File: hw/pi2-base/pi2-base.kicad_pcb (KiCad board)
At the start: 2 copper layers, 100 x 125 mm, 81 parts, among them J1 WAGO 2081-1122, J10 BUS Pull-down, J11 JUMPER3, J12 JUMPER3, J13 Power LEDs, J14 JUMPER3, J15 JUMPER3, J16 JUMPER3, J17 JUMPER3, J2 WAGO 243 orange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

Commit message: pi2-base revision 1 (prototypes ordered)
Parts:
- L1: value 220uH -> 100uH
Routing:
- net GND: track 0.00 -> 26.4 mm, vias 0 -> 9
- net (no net): track 5.74 -> 0.00 mm, vias 8 -> 0
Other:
- net class Power: via_dia 1 -> 1.2

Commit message: Changed resistor values from 56k/100k to 10k/18k of voltage divider of TXD and CTS
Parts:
- R10, R9: value 100k -> 18k
- R6, R7: value 56k -> 10k
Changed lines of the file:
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@@
-(kicad_pcb (version 20160815) (host pcbnew no-vcs-found)
+(kicad_pcb (version 20170123) (host pcbnew no-vcs-found-7600~57~ubuntu14.04.1)
   (general
     (links 173)
     (no_connects 0)
-    (area 73.305715 20.28 207.305716 164.789908)
+    (area 95.944999 32.404999 196.095001 157.555001)
     (thickness 1.6)
     (drawings 59)
@@
     (uvia_dia 0.3)
     (uvia_drill 0.1)
-    (diff_pair_gap 0.25)
-    (diff_pair_width 0.2)
     (add_net "/2 Relays/LEDVCC")
     (add_net "/2 Relays/REL1")
@@
     (uvia_dia 0.3)
     (uvia_drill 0.1)
-    (diff_pair_gap 0.25)
-    (diff_pair_width 0.2)
     (add_net /REL1_COM)
     (add_net /REL1_NC)
@@
     (uvia_dia 0.3)
     (uvia_drill 0.1)
-    (diff_pair_gap 0.25)
-    (diff_pair_width 0.2)
     (add_net +24V)
     (add_net +3.3V)
@@
       (effects (font (size 0.8 0.8) (thickness 0.15)) (justify mirror))
     )
-    (fp_text value 56k (at 0.127 -1.524 270) (layer B.Fab)
+    (fp_text value 10k (at 0.127 -1.524 270) (layer B.Fab)
       (effects (font (size 0.8 0.8) (thickness 0.15)) (justify mirror))
     )
@@
       (effects (font (size 0.8 0.8) (thickness 0.15)) (justify mirror))
     )
-    (fp_text value 56k (at 0.127 -1.524 270) (layer B.Fab)
+    (fp_text value 10k (at 0.127 -1.524 270) (layer B.Fab)
       (effects (font (size 0.8 0.8) (thickness 0.15)) (justify mirror))
     )
@@
       (effects (font (size 0.8 0.8) (thickness 0.15)) (justify mirror))
     )
-    (fp_text value 100k (at 0.127 -1.524 270) (layer B.Fab)
+    (fp_text value 18k (at 0.127 -1.524 270) (layer B.Fab)
       (effects (font (size 0.8 0.8) (thickness 0.15)) (justify mirror))
     )
@@
       (effects (font (size 0.8 0.8) (thickness 0.15)) (justify mirror))
     )
-    (fp_text value 100k (at 0.127 -1.524 270) (layer B.Fab)
-      (effects (font (size 0.8 0.8) (thickness 0.15)) (justify mirror))
-    )
+    (fp_text value 18k (at 0.127 -1.524 270) (layer B.Fab)
+      (effects (font (size 0.8 0.8) (thickness 0.15)) (justify mirror))
+    )

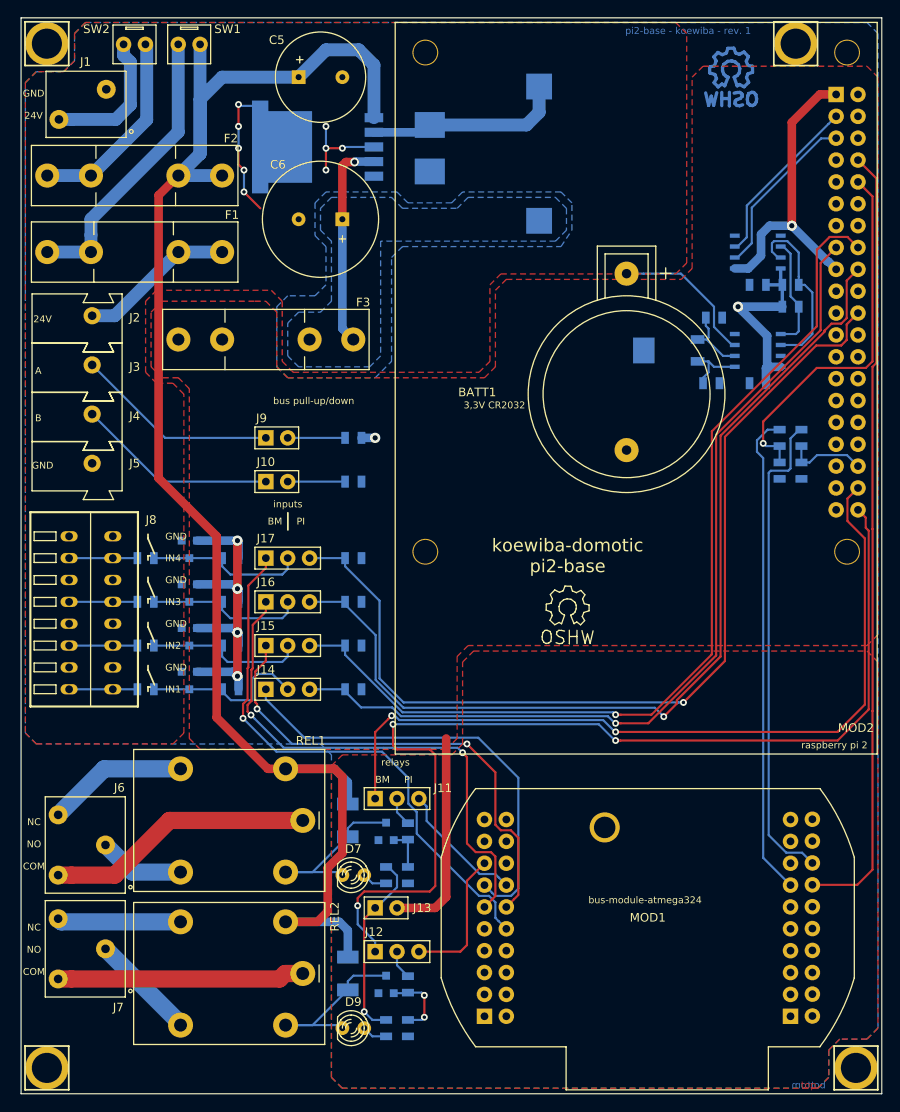
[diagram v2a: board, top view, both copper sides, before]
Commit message: Fix: Silkscreen jumper description Fix: Relay pinout
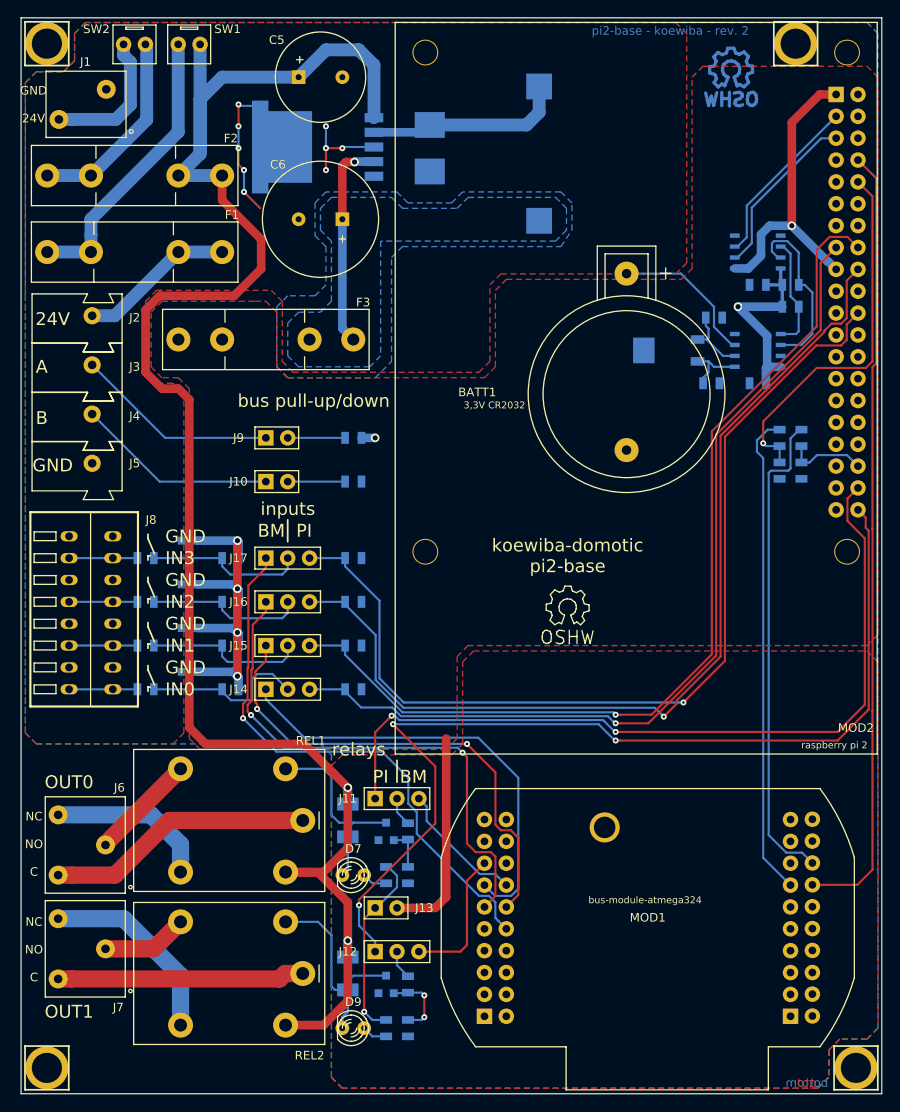
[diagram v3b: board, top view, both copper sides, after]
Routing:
- net +24V: track 183.9 -> 206.1 mm, vias 0 -> 2
- net /REL2_NC: track 14.4 -> 22.9 mm
- net /PI_REL2: track 121.0 -> 114.2 mm
- net Net-(D8-Pad1): track 21.4 -> 24.9 mm
- net Net-(D6-Pad1): track 21.4 -> 24.0 mm
- net /REL2_NO: track 12.5 -> 10.0 mm
- net /REL1_NO: track 10.0 -> 12.5 mm
- net /REL1_NC: track 16.4 -> 18.9 mm
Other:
- net class Default: trace_width 0.25 -> 0.3; via_dia 0.8 -> 0.7
- net class Power: clearance 0.4 -> 0.2; via_dia 1.2 -> 1
- board text added: "2018-06-12 Fix: Relay footprint pin assignment Fix: Silkscreen text for relay jumpers"
- board text added: "Do not use relays for 230V! 48V max!"
- board text added: "IN0"
- board text added: "NC NO C"
- board text added: "OUT0"
- board text added: "OUT1"
- board text added: "pi2-base - koewiba - rev. 2"
- board text removed: "IN4"
- board text removed: "NC NO COM"
- board text removed: "pi2-base - koewiba - rev. 1"

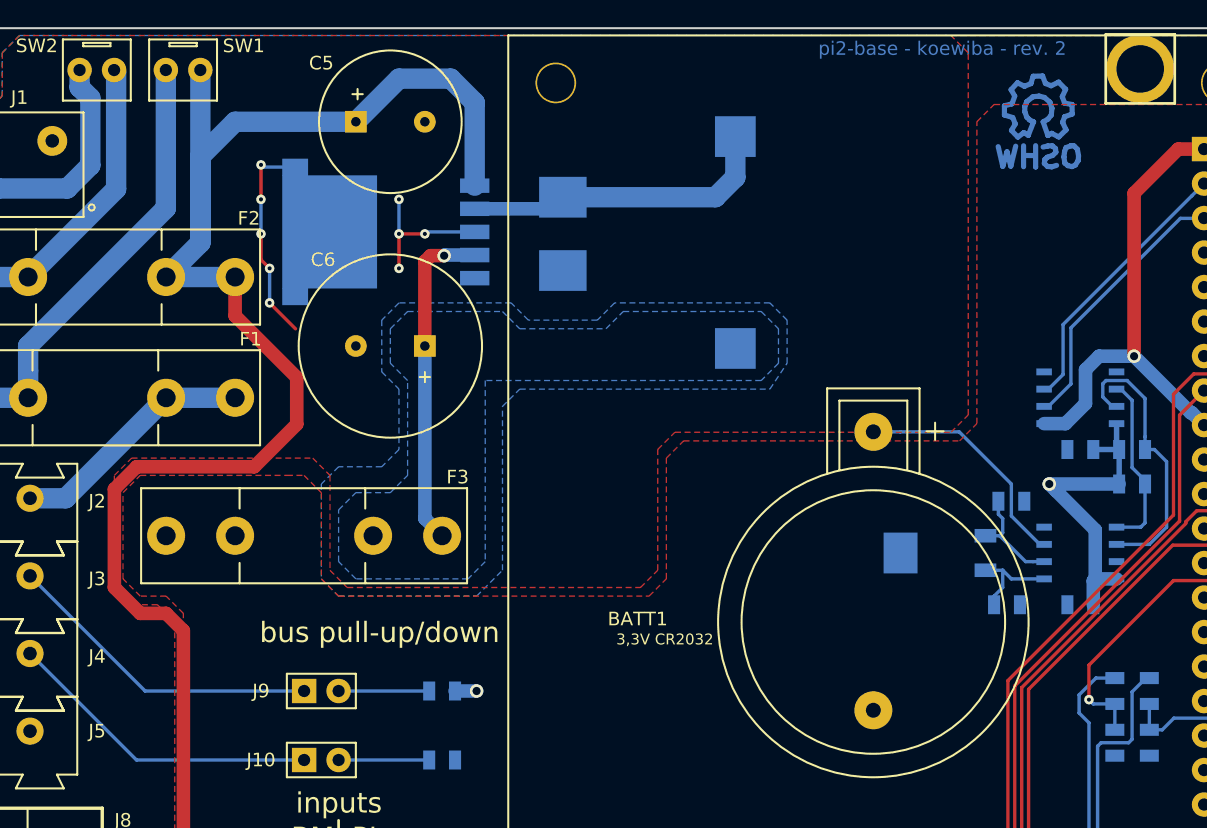
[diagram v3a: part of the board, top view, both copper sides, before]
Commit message: Renamed Rev2 -> RevB Updated 3d footprints Replaced busmodule RevA with RevB symbol
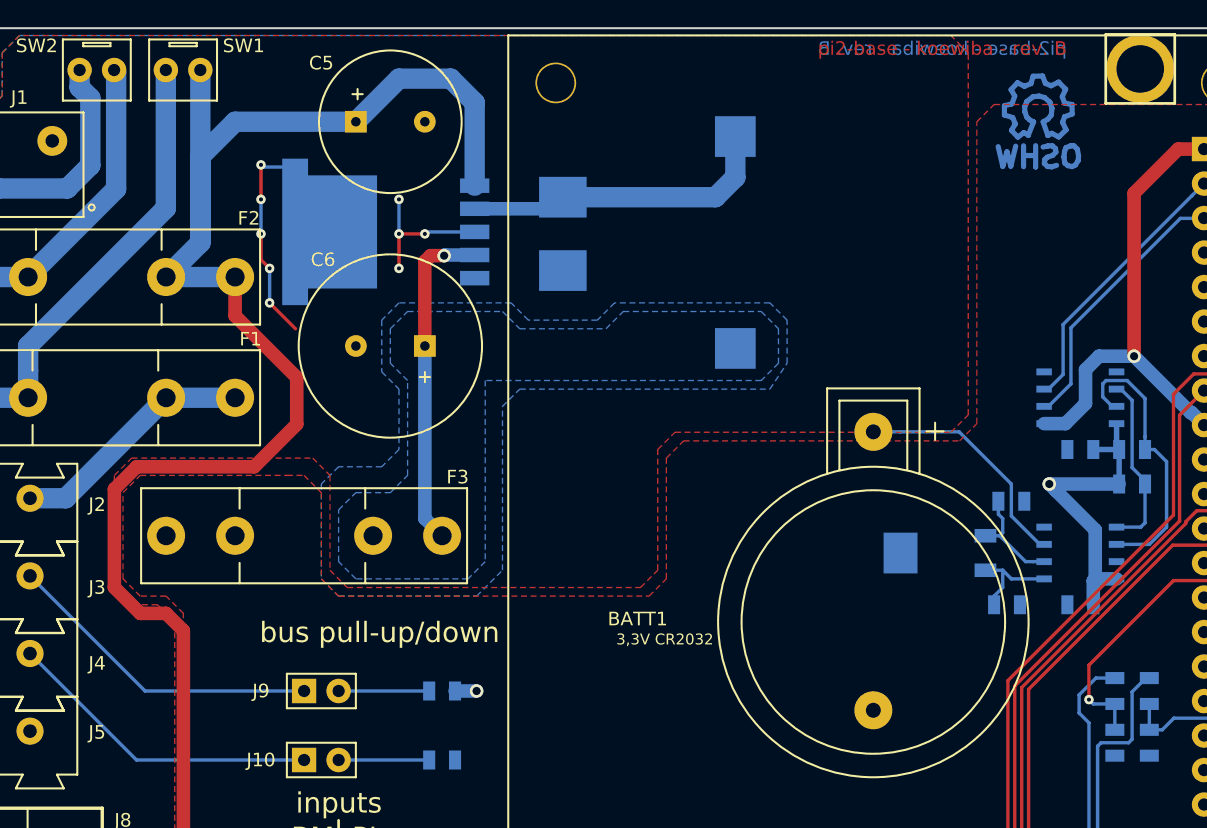
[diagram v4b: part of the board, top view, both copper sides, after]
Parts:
- J2, J3, J4, J5: footprint Connector_WAGO:WAGO_243 -> Connector_WAGO:WAGO243
- MOD1: value bus-module_atmega324 -> bus-module_atmega324_revB
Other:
- board text added: "pi2-base - koewiba - rev. B"
- board text removed: "pi2-base - koewiba - rev. 2"

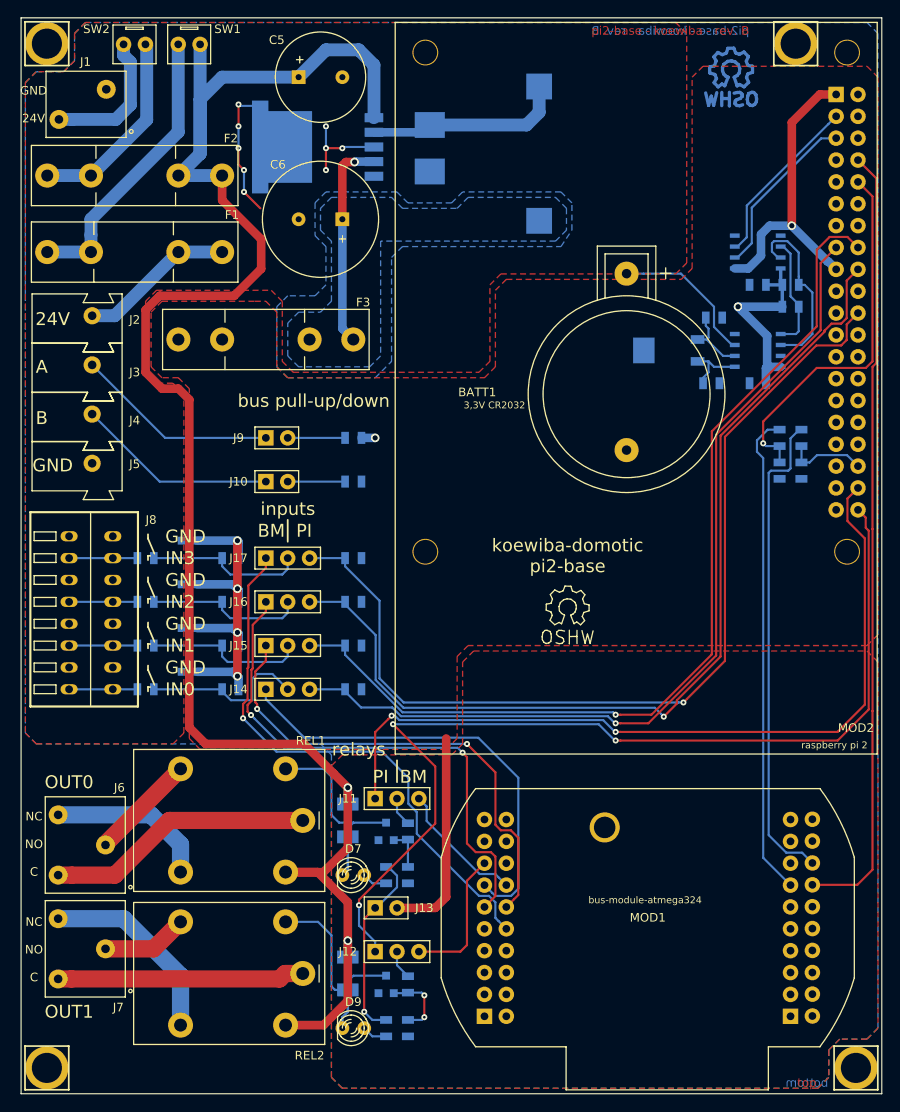
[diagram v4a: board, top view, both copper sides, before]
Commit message: Update to KiCAD6: pi2-base
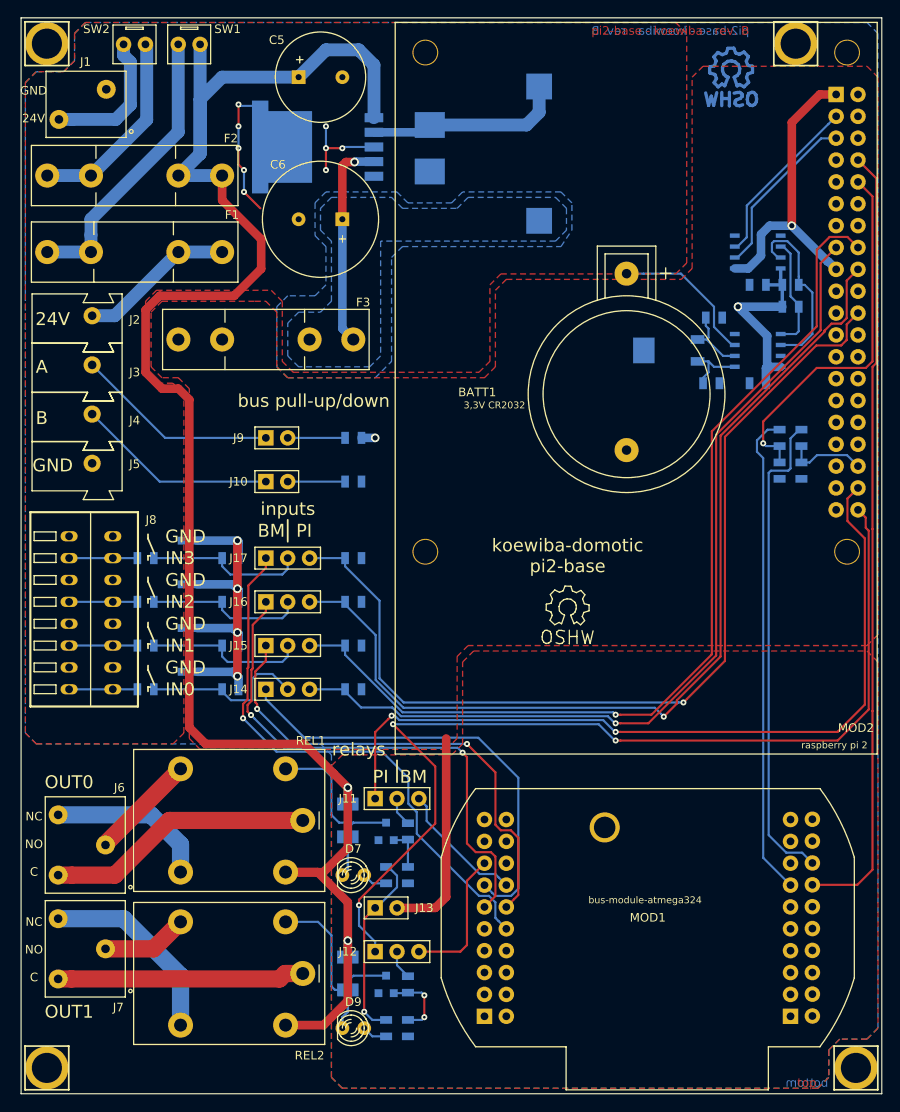
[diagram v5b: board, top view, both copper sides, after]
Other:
- net class 230V removed
- net class Default removed
- net class Power removed
